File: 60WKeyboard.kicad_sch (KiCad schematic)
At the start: 54 parts, among them IC1 USBLC6-2SC6, J1 Conn_01x02, J2 USB4215-03-A_REVA, SW1 RotaryEncoder, U1 NRF54L15-QFAA-R, Y1 ABM11W-32.0000MHZ-7-D1X-T3, Y2 ECS-.327-7-12-TR

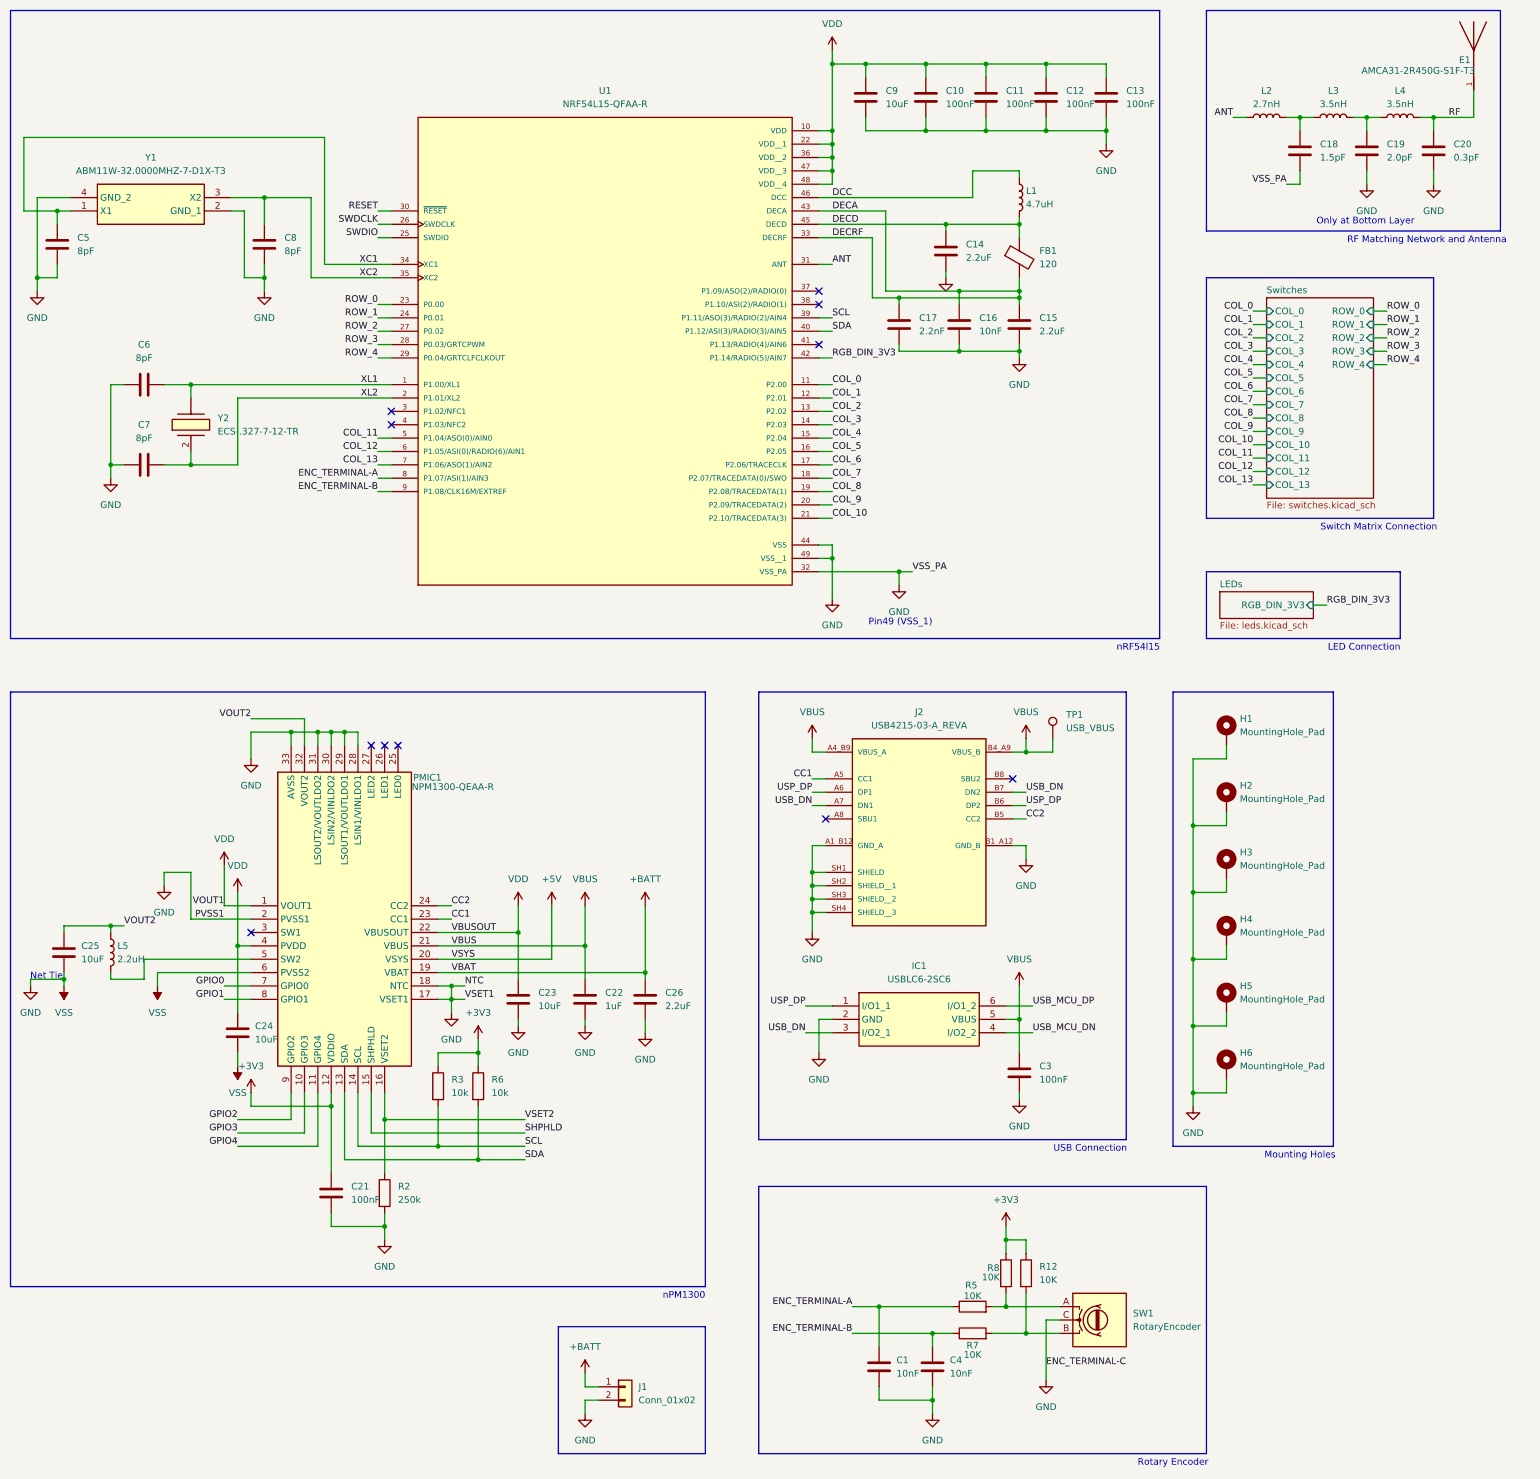
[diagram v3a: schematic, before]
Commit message: created v0.2 pcb
Started work on v0.2 pcb. Placed switches, LEDS, and Diodes. Working on MCU routing
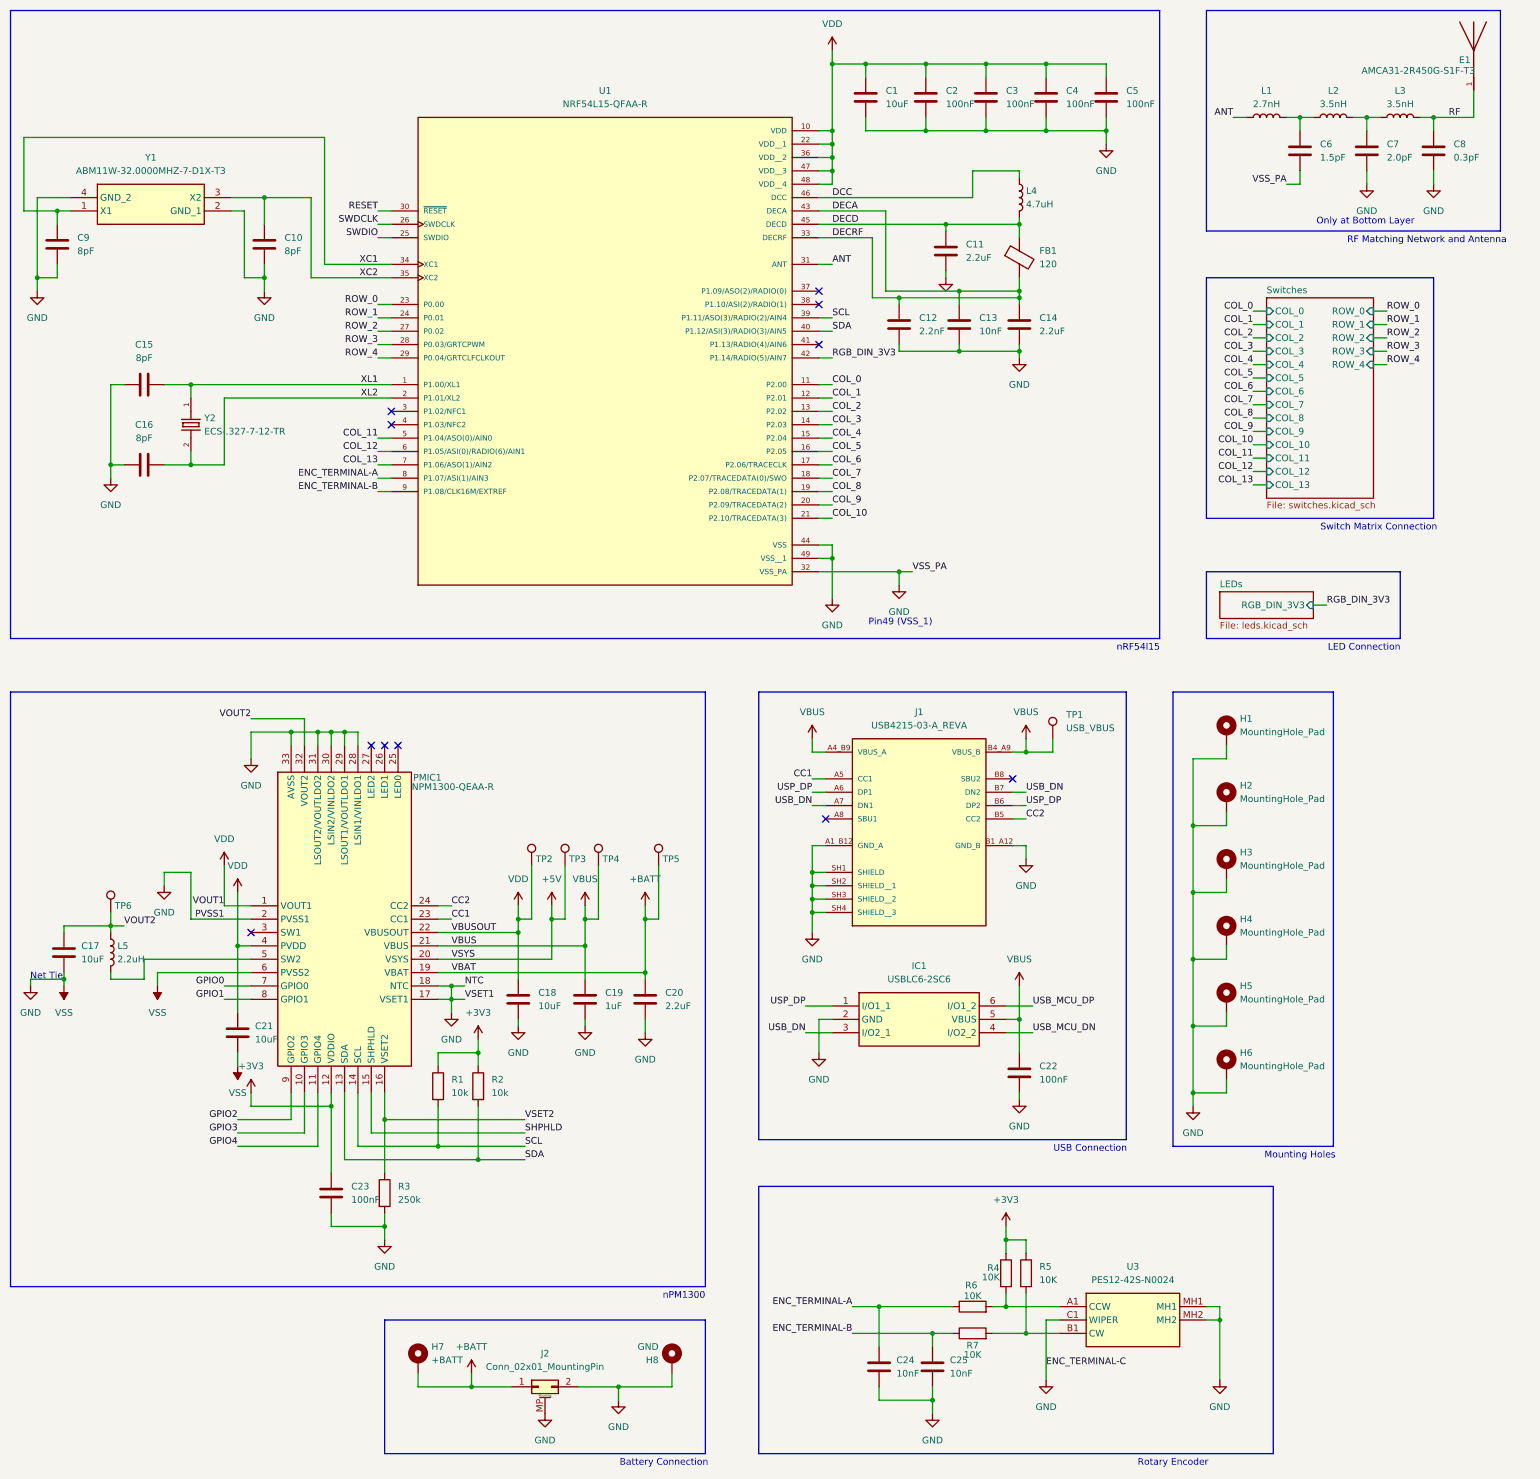
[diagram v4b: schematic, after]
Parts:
- removed J1: Conn_01x02, Connector_JST:JST_PH_S2B-PH-SM4-TB_1x02-1MP_P2.00mm_Horizontal, symbol Connector_Generic:Conn_01x02
- removed SW1: RotaryEncoder, Rotary_Encoder:RotaryEncoder_Bourns_Horizontal_PEC09-2xxxF-Nxxxx, symbol Device:RotaryEncoder
- removed Y2: ECS-.327-7-12-TR, ECS327712TR, symbol SamacSys_Parts:ECS-.327-7-12-TR
- added H7: +BATT, TestPoint:TestPoint_THTPad_D2.5mm_Drill1.2mm, symbol Mechanical:MountingHole_Pad
- added H8: GND, TestPoint:TestPoint_THTPad_2.5x2.5mm_Drill1.2mm, symbol Mechanical:MountingHole_Pad
- added J2: Conn_02x01_MountingPin, Connector_JST:JST_PH_S2B-PH-SM4-TB_1x02-1MP_P2.00mm_Horizontal, symbol Connector_Generic_MountingPin:Conn_02x01_MountingPin
- added TP2: VBUSOUT, TestPoint:TestPoint_Pad_D2.0mm, symbol Connector:TestPoint
- added TP3: 5V, TestPoint:TestPoint_Pad_D2.0mm, symbol Connector:TestPoint
- added TP4: VBUS, TestPoint:TestPoint_Pad_D2.0mm, symbol Connector:TestPoint
- added TP5: VBAT, TestPoint:TestPoint_Pad_D2.0mm, symbol Connector:TestPoint
- added TP6: USB_VBUS, TestPoint:TestPoint_Pad_D2.0mm, symbol Connector:TestPoint
- added U3: PES12-42S-N0024, SamacSys_Parts:PES1242SN0024, symbol SamacSys_Parts:PES12-42S-N0024
- added Y2: ECS-.327-7-12-TR, SamacSys_Parts:XTAL_ECS-.327-7-12-TR, symbol ECS-.327-7-12-TR:ECS-.327-7-12-TR
- C1: renamed from C9; footprint (none) -> Capacitor_SMD:C_0603_1608Metric
- C10: renamed from C8; footprint (none) -> Capacitor_SMD:C_0402_1005Metric
- C11: renamed from C14; footprint (none) -> Capacitor_SMD:C_0402_1005Metric
- C12: renamed from C17; footprint (none) -> Capacitor_SMD:C_0402_1005Metric
- C13: renamed from C16; footprint (none) -> Capacitor_SMD:C_0402_1005Metric
- C14: renamed from C15; footprint (none) -> Capacitor_SMD:C_0402_1005Metric
- C15: renamed from C6; footprint (none) -> Capacitor_SMD:C_0402_1005Metric
- C16: renamed from C7; footprint (none) -> Capacitor_SMD:C_0402_1005Metric
- C17: renamed from C25; footprint (none) -> Capacitor_SMD:C_0603_1608Metric
- C18: renamed from C23; footprint (none) -> Capacitor_SMD:C_0603_1608Metric
- C19: renamed from C22; footprint (none) -> Capacitor_SMD:C_0603_1608Metric
- C2: renamed from C10; footprint (none) -> Capacitor_SMD:C_0402_1005Metric
- C20: renamed from C26; footprint (none) -> Capacitor_SMD:C_0402_1005Metric
- C21: renamed from C24; footprint (none) -> Capacitor_SMD:C_0603_1608Metric
- C22: renamed from C3; footprint (none) -> Capacitor_SMD:C_0402_1005Metric
- C23: renamed from C21; footprint (none) -> Capacitor_SMD:C_0402_1005Metric
- C3: renamed from C11; footprint (none) -> Capacitor_SMD:C_0402_1005Metric
- C4: renamed from C12; footprint (none) -> Capacitor_SMD:C_0402_1005Metric
- C5: renamed from C13; footprint (none) -> Capacitor_SMD:C_0402_1005Metric
- C6: renamed from C18; footprint (none) -> Capacitor_SMD:C_0201_0603Metric
- C7: renamed from C19; footprint (none) -> Capacitor_SMD:C_0201_0603Metric
- C8: renamed from C20; footprint (none) -> Capacitor_SMD:C_0201_0603Metric
- C9: renamed from C5; footprint (none) -> Capacitor_SMD:C_0402_1005Metric
- E1: footprint AMCA31-2R450G-S1F-T3:XDCR_AMCA31-2R450G-S1F-T3 -> SamacSys_Parts:XDCR_AMCA31-2R450G-S1F-T3
- FB1: footprint (none) -> Inductor_SMD:L_0402_1005Metric
- H1, H2, H3, H4, H5, H6: footprint (none) -> MountingHole:MountingHole_2.2mm_M2_Pad
- IC1: footprint SOT95P280X145-6N -> SamacSys_Parts:SOT95P280X145-6N
- J1: renamed from J2; footprint USB4215-03-A_REVA:GCT_USB4215-03-A_REVA -> SamacSys_Parts:GCT_USB4215-03-A_REVA
- L1: renamed from L2; footprint (none) -> Inductor_SMD:L_0201_0603Metric
- L2: renamed from L3; footprint (none) -> Inductor_SMD:L_0201_0603Metric
- L3: renamed from L4; footprint (none) -> Inductor_SMD:L_0201_0603Metric
- L4: renamed from L1; footprint (none) -> Inductor_SMD:L_0603_1608Metric
- L5: footprint (none) -> Inductor_SMD:L_0805_2012Metric
- PMIC1: footprint QFN50P500X500X90-33N -> SamacSys_Parts:QFN50P500X500X90-33N
- R1: renamed from R3; footprint (none) -> Resistor_SMD:R_0402_1005Metric
- R2: renamed from R6; footprint (none) -> Resistor_SMD:R_0402_1005Metric
- R3: renamed from R2; footprint (none) -> Resistor_SMD:R_0805_2012Metric
- R4: renamed from R8; footprint SamacSys_Parts:RESC1005X40N -> Resistor_SMD:R_0402_1005Metric
- R5: renamed from R12; footprint SamacSys_Parts:RESC1005X40N -> Resistor_SMD:R_0402_1005Metric
- R6: renamed from R5; footprint SamacSys_Parts:RESC1005X40N -> Resistor_SMD:R_0402_1005Metric
- R7: footprint SamacSys_Parts:RESC1005X40N -> Resistor_SMD:R_0402_1005Metric
- TP1: footprint (none) -> TestPoint:TestPoint_Pad_D2.0mm
- U1: footprint NRF54L15-QFAA-R:QFN40P600X600X90-49N -> SamacSys_Parts:QFN40P600X600X90-49N
- Y1: footprint ABM11W300000MHZ4B1UT3 -> SamacSys_Parts:ABM11W300000MHZ4B1UT3
- renumbered C1 to C24, C4 to C25
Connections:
- net +5V: now also TP3.1
- net +BATT: now also H7.1, J2.1 (Pin_1), TP5.1
- net GND: now also H8.1, J2.2 (Pin_2), J2.MP (MountPin), U3.C1 (WIPER), U3.MH1, U3.MH2
- net VBUS: now also TP4.1
- net VDD: now also TP2.1
- net VOUT2: now also TP6.1
- net XL1: now also Y2.1
- net XL2: now also Y2.2
- net at R4.2, R6.2: now also U3.A1 (CCW)
- net at R5.2, R7.2: now also U3.B1 (CW)
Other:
- note added: "Battery Connection"

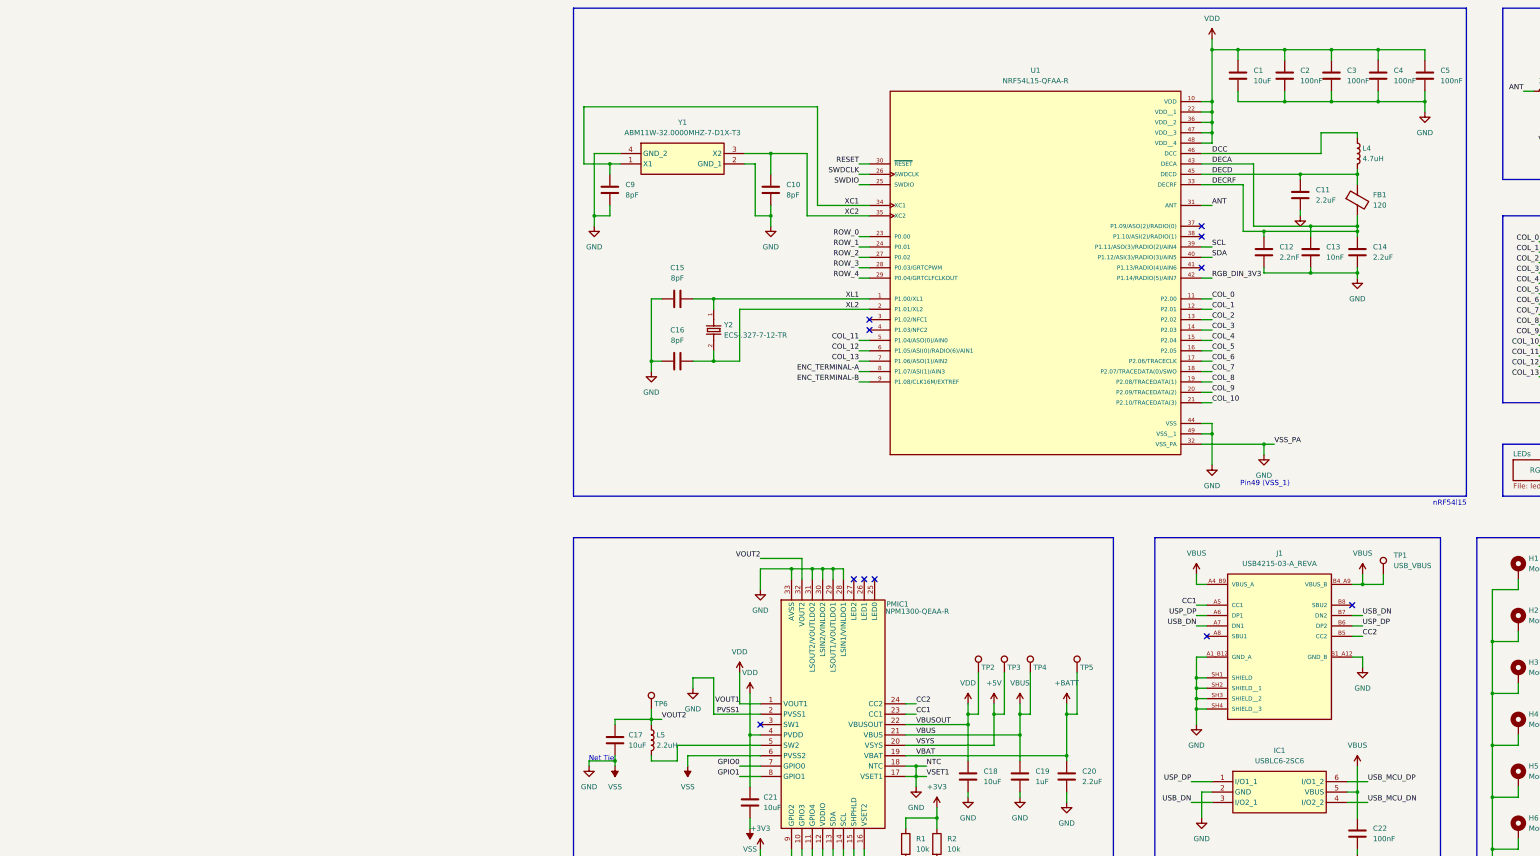
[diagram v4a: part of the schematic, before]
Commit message: v0.2 in dev
MCU change because im stupid and now I have to redo rf. Routed columns. Started routing USB port.
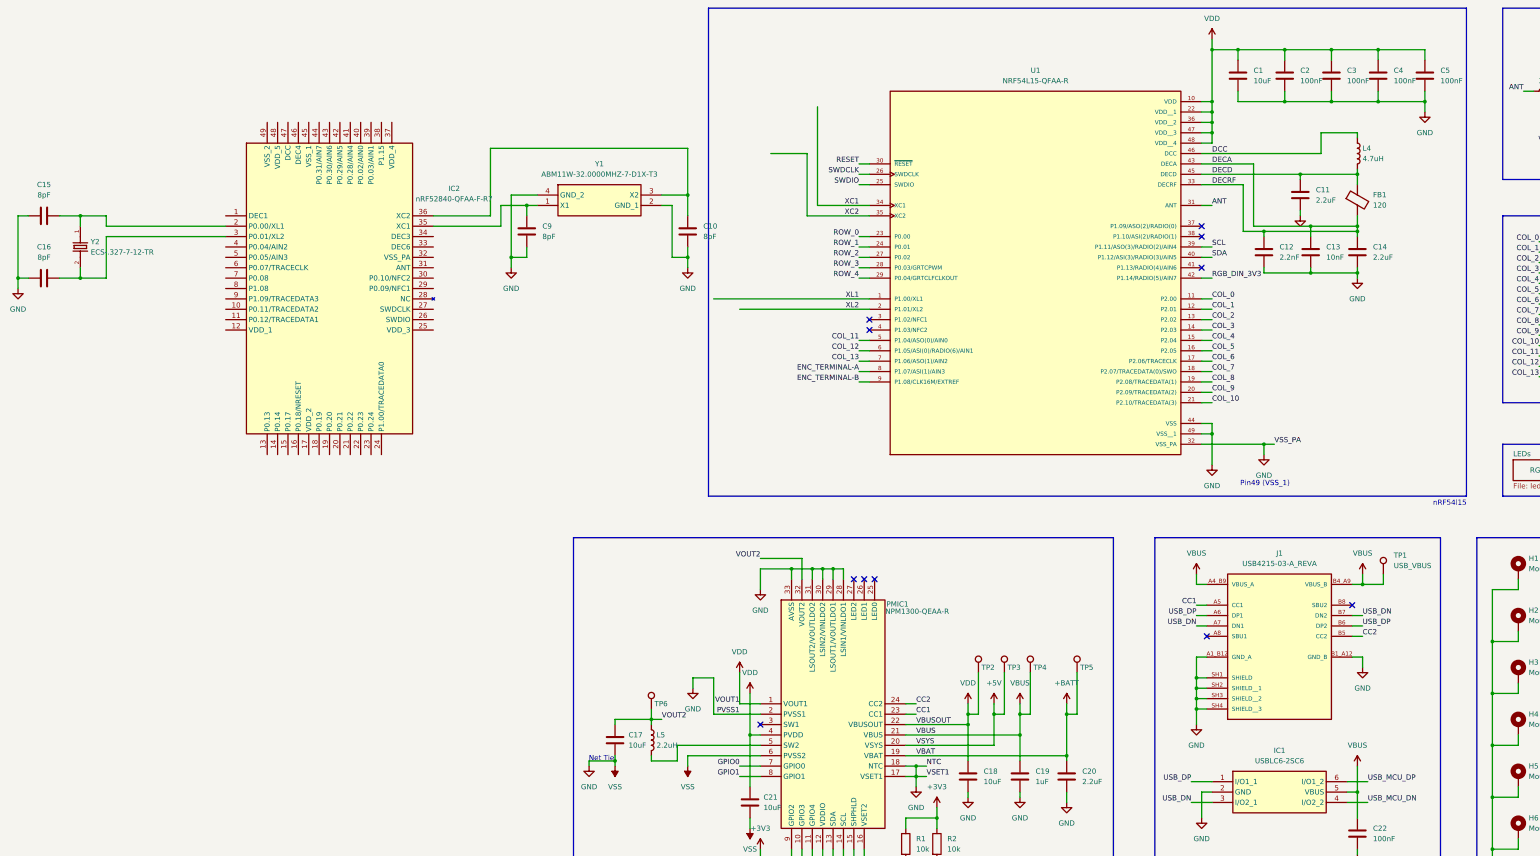
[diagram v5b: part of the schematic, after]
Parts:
- added IC2: nRF52840-QFAA-F-R7, QFN40P600X600X95-49N-D, symbol SamacSys_Parts:nRF52840-QFAA-F-R7
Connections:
- net XC1: no longer C9.1, Y1.1 (X1)
- net XC2: no longer C10.1, Y1.3 (X2)
- net XL1: no longer C15.2, Y2.1
- net XL2: no longer C16.2, Y2.2
- net USP_DP renamed USB_DP
- new net: C9.1, IC2.35 (XC1), Y1.1 (X1)
- new net: C15.2, IC2.2 (P0.00/XL1), Y2.1
- new net: C16.2, IC2.3 (P0.01/XL2), Y2.2
- new net: C10.1, IC2.36 (XC2), Y1.3 (X2)
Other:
- moved on the sheet: C10, C15, C16, C9, Y1, Y2
